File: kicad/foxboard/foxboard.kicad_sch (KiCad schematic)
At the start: 183 parts, among them J2 USB_C_Receptacle_USB2.0, K1 KEYSW, K10 KEYSW, K11 KEYSW, K12 KEYSW, K13 KEYSW, K14 KEYSW, K15 KEYSW, K16 KEYSW, K17 KEYSW, K18 KEYSW, K19 KEYSW, K2 KEYSW, K20 KEYSW, K21 KEYSW, K22 KEYSW, K23 KEYSW, K24 KEYSW, K25 KEYSW, K26 KEYSW, K27 KEYSW, K28 KEYSW, K29 KEYSW, K3 KEYSW, K30 KEYSW, K31 KEYSW, K32 KEYSW, K33 KEYSW, K34 KEYSW, K35 KEYSW, K36 KEYSW, K37 KEYSW, K38 KEYSW, K39 KEYSW, K4 KEYSW, K40 KEYSW, K41 KEYSW, K42 KEYSW, K43 KEYSW, K44 KEYSW, K45 KEYSW, K46 KEYSW, K47 KEYSW, K48 KEYSW, K49 KEYSW, K5 KEYSW, K50 KEYSW, K51 KEYSW, K52 KEYSW, K53 KEYSW, K54 KEYSW, K55 KEYSW, K56 KEYSW, K57 KEYSW, K58 KEYSW, K59 KEYSW, K6 KEYSW, K60 KEYSW, K61 KEYSW, K62 KEYSW, K63 KEYSW, K64 KEYSW, K65 KEYSW, K66 KEYSW, K67 KEYSW, K68 KEYSW, K69 KEYSW, K7 KEYSW, K70 KEYSW, K71 KEYSW, K72 KEYSW, K73 KEYSW, K74 KEYSW, K75 KEYSW, K76 KEYSW, K77 KEYSW, K78 KEYSW, K79 KEYSW, K8 KEYSW, K80 KEYSW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

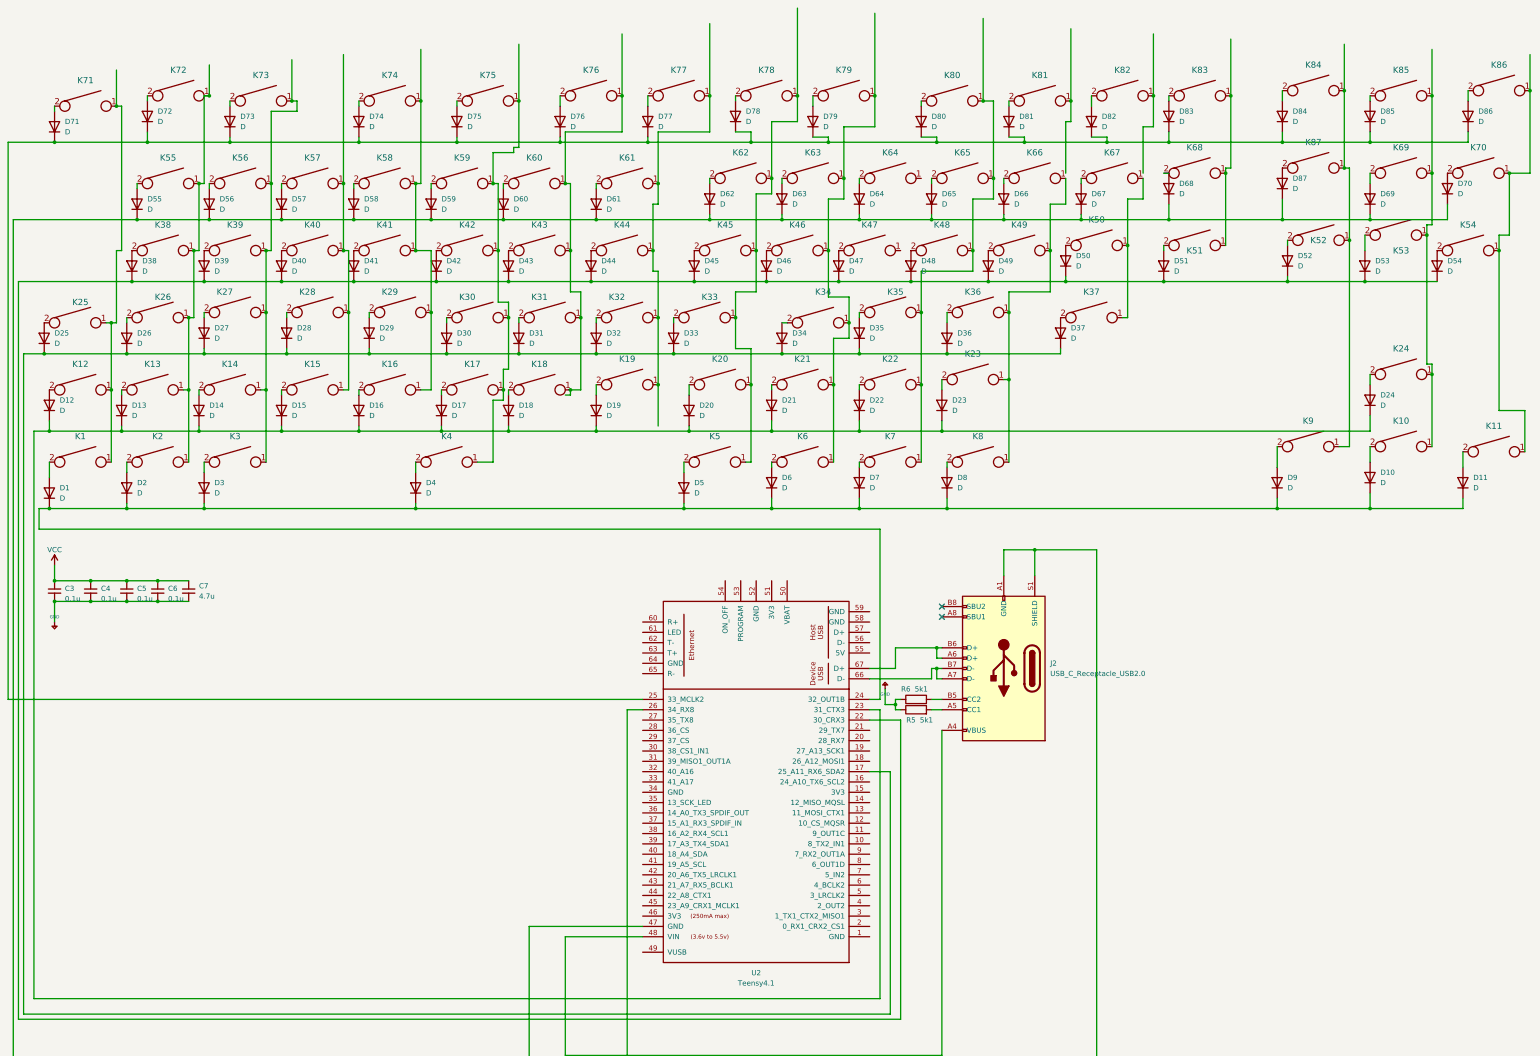
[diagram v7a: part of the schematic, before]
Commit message: add few rows update eeschema
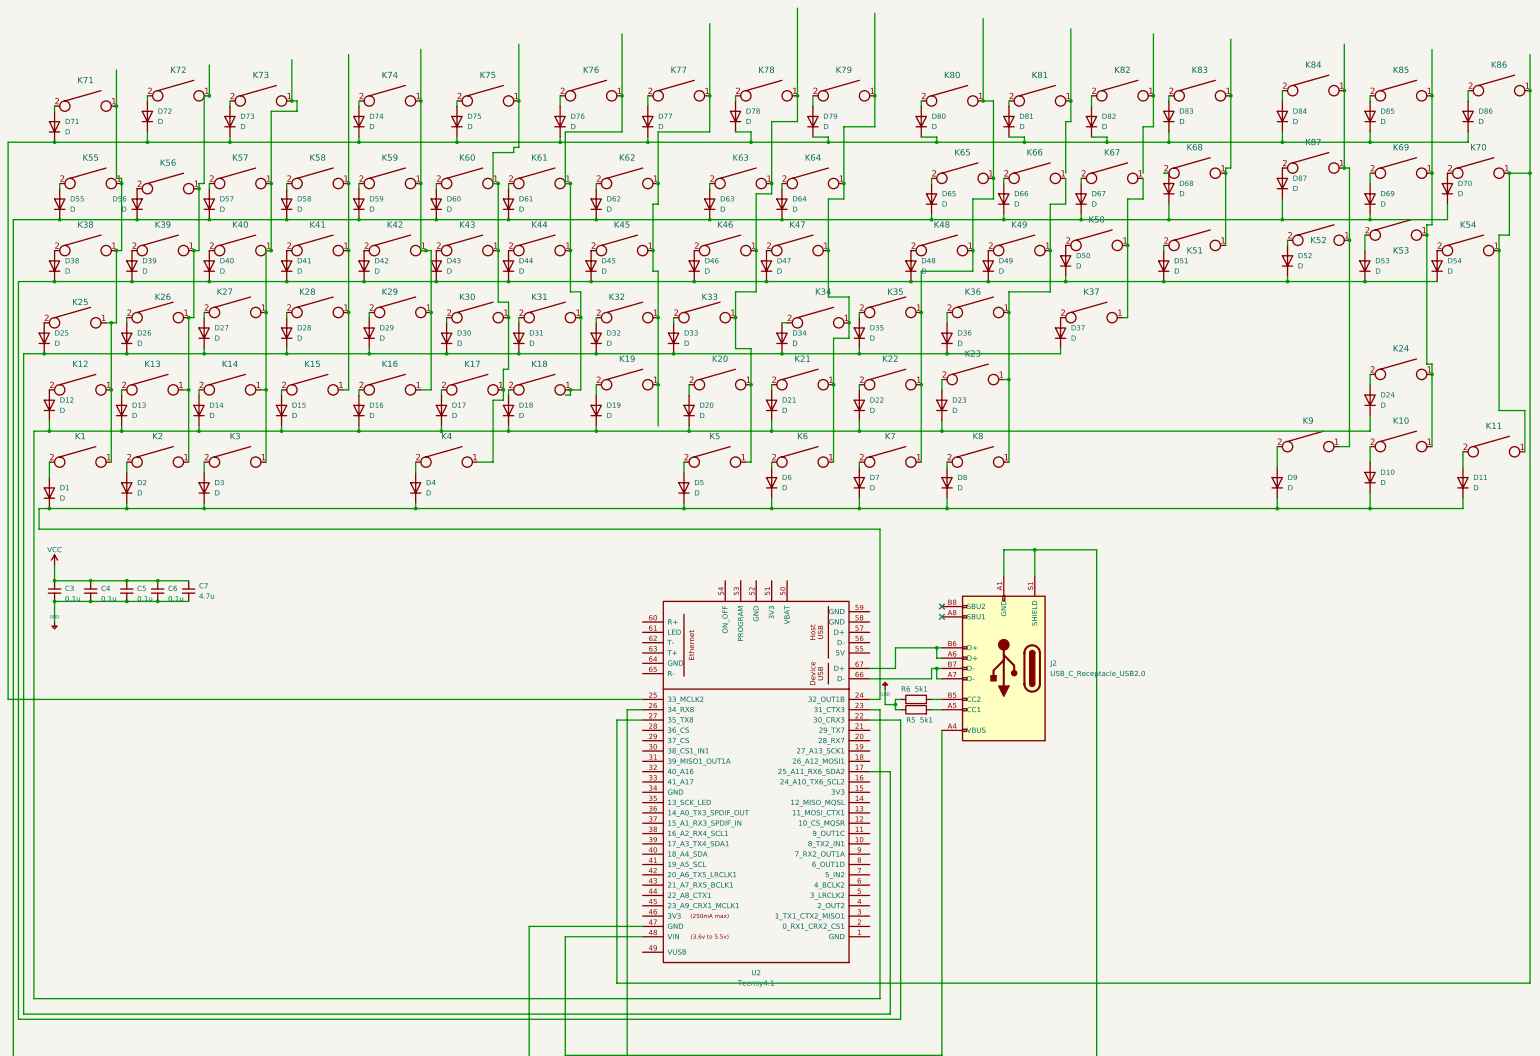
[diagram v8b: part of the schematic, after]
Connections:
- net at K11.1, K54.1, K70.1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: now also U2.27 (35_TX8)
- net at K14.1, K27.1, K3.1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: now also K40.1, K57.1; no longer K39.1, K56.1
- net at K20.1, K33.1, K5.1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: now also K46.1, K63.1; no longer K45.1, K62.1
- net at K21.1, K34.1, K6.1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: now also K47.1, K64.1; no longer K46.1, K63.1
- net at K1.1, K12.1, K25.1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: now also K38.1, K55.1
- net at K18.1, K31.1, K76.1: now also K44.1, K61.1; no longer K43.1, K60.1
- net at K19.1, K32.1, K77.1: now also K45.1, K62.1; no longer K44.1, K61.1
- net at K13.1, K2.1, K26.1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: now also K39.1, K56.1; no longer K38.1, K55.1
- net at K16.1, K29.1, K74.1: now also K42.1, K59.1; no longer K41.1, K58.1
- net at K15.1, K28.1: now also K41.1, K58.1; no longer K40.1, K57.1
- net at K17.1, K30.1, K4.1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: now also K43.1, K60.1; no longer K42.1, K59.1
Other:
- moved on the sheet: D40, D41, D42, D43, D44, D45, D46, D47, D57, D58, D59, D60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
